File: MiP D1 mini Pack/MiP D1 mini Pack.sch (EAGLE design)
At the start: 6 parts, among them J2 D1 mini, J3 Debug

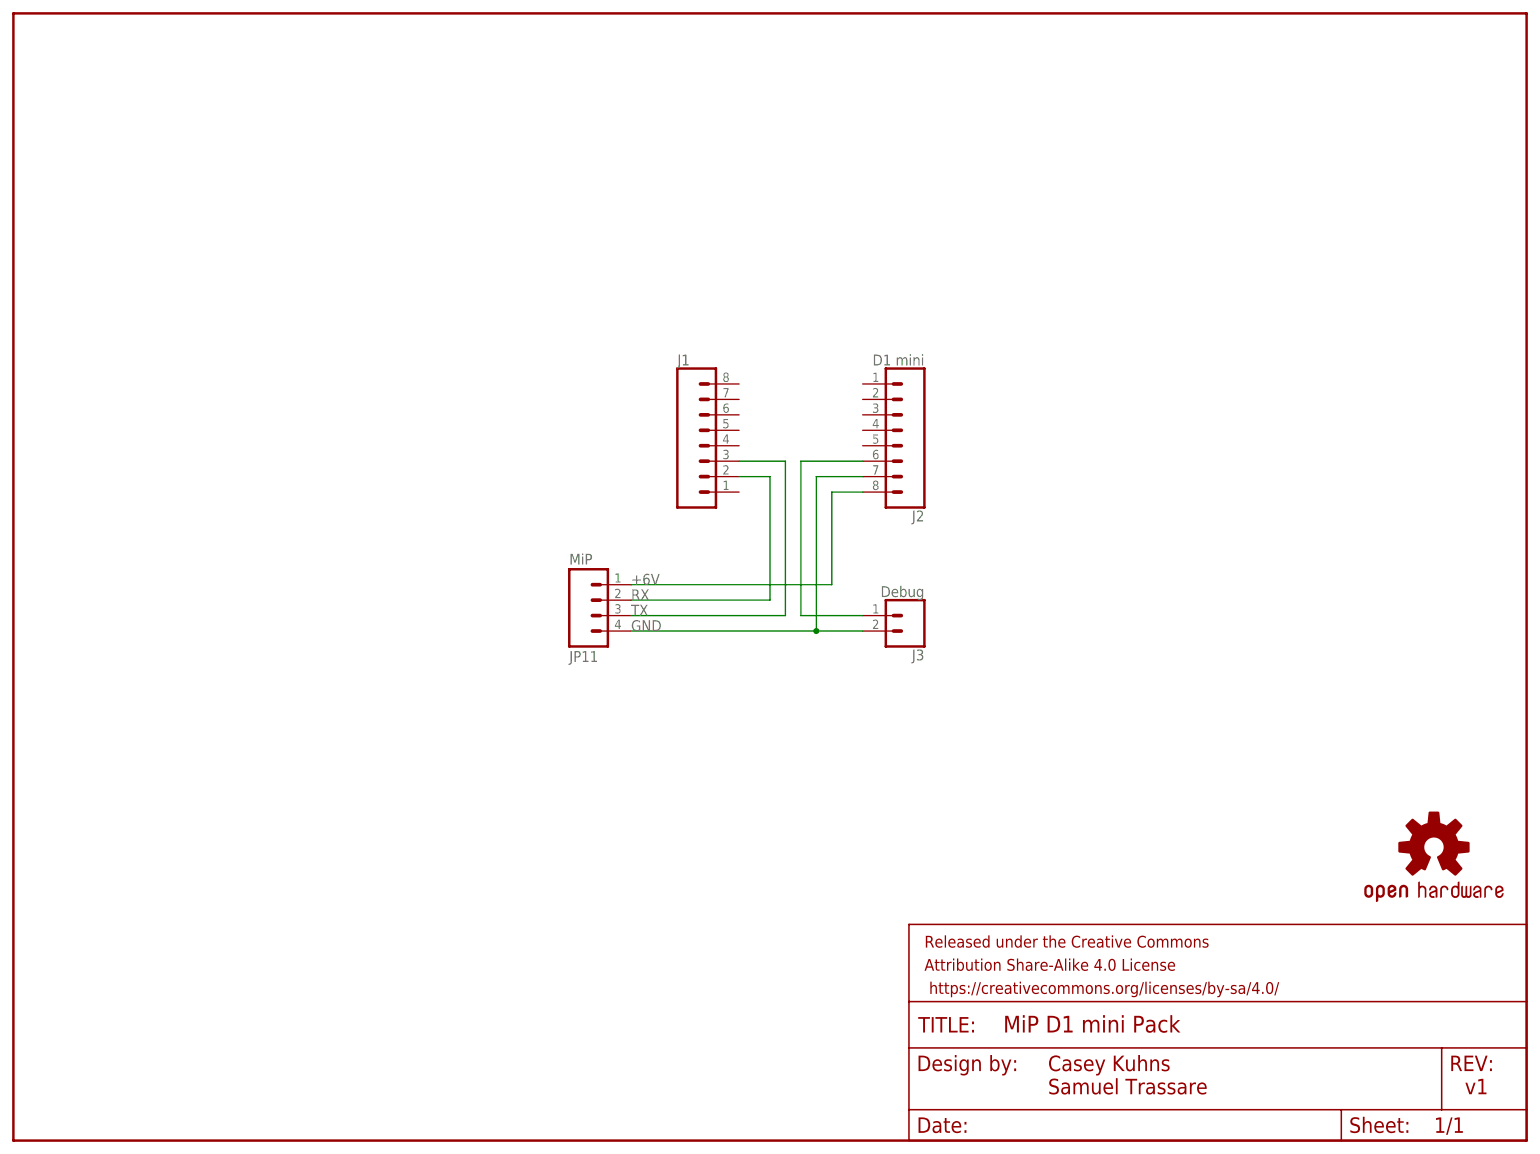
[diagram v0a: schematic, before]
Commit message: Fixed rookie mistake (RX/TX was backwards)
Fixed twisted RX/TX pair, corrected labels, added labels for debug
connector, made minor moves.
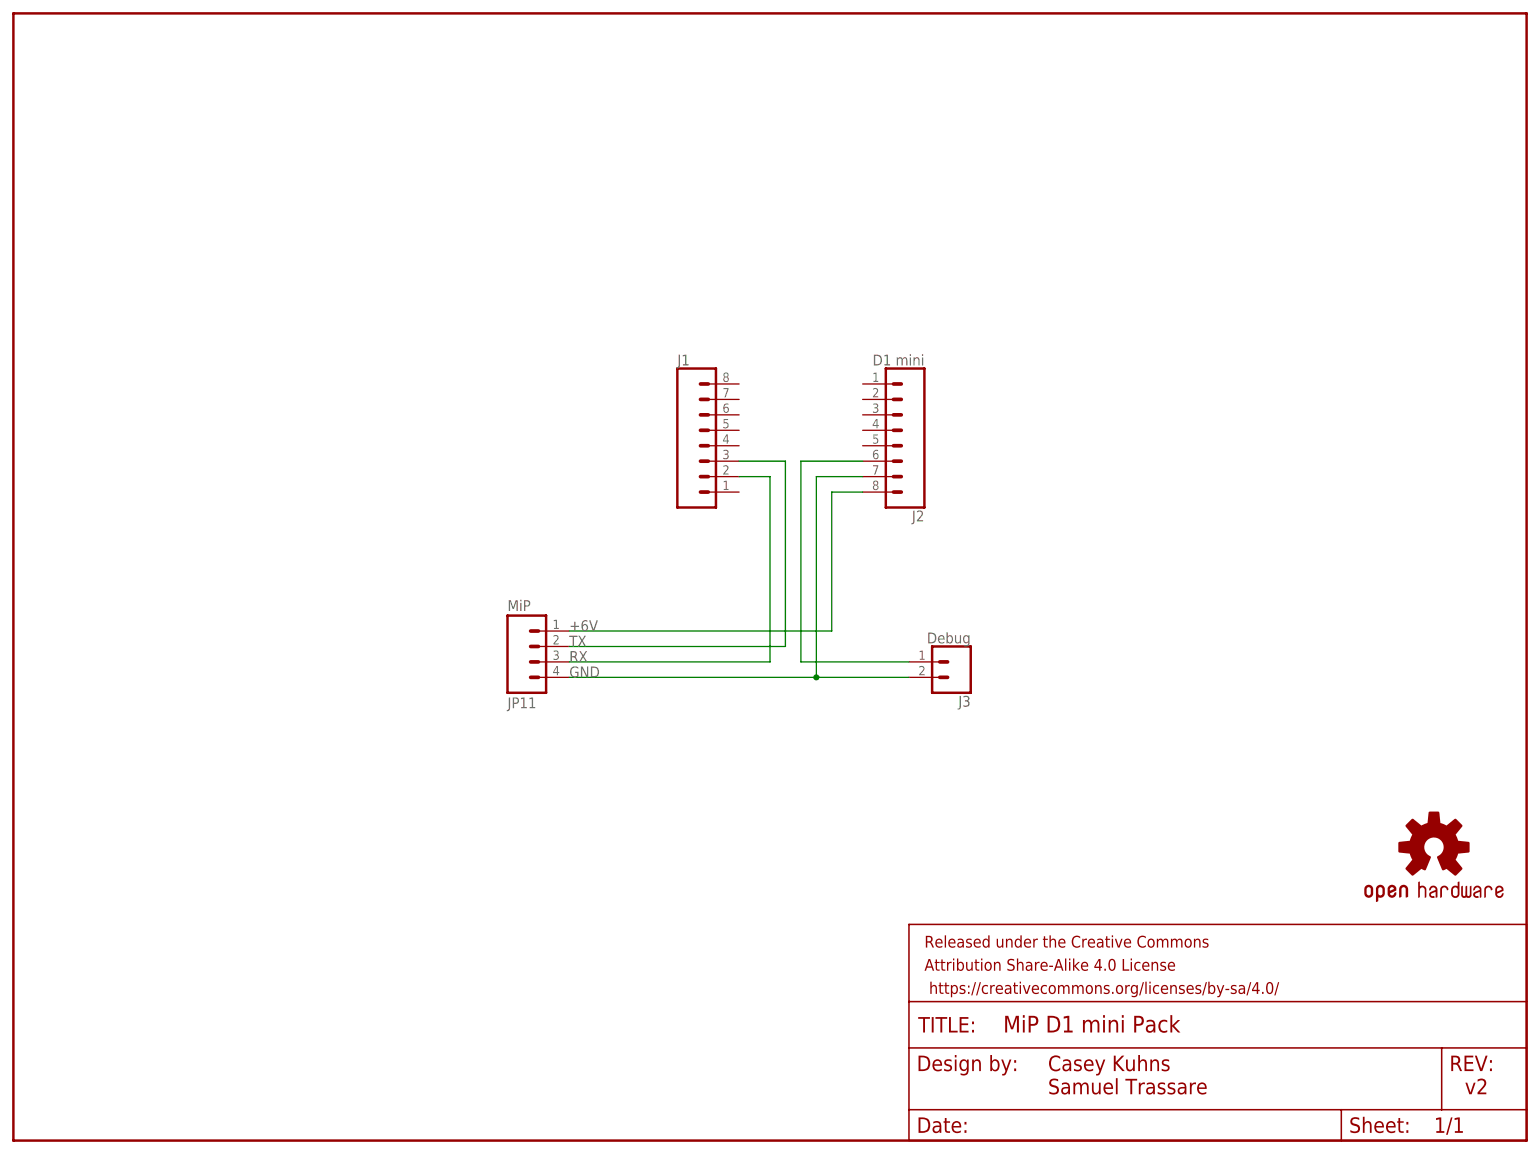
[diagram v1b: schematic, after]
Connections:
- net N$4 renamed DEBUG
- net RX: now also JP11.3; no longer JP11.2
- net TX: now also JP11.2; no longer JP11.3
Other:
- note added: "v2"
- note removed: "v1"
- moved on the sheet: J3, JP11
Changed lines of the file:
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@@
 <text x="170.18" y="7.62" size="2.54" layer="94">Casey Kuhns
 Samuel Trassare</text>
-<text x="238.76" y="7.62" size="2.54" layer="94">v1</text>
+<text x="238.76" y="7.62" size="2.54" layer="94">v2</text>
 </plain>
 <instances>
 <instance part="FRAME1" gate="G$1" x="0" y="0"/>
 <instance part="FRAME1" gate="G$2" x="147.32" y="0"/>
-<instance part="JP11" gate="G$1" x="96.52" y="88.9" rot="MR180"/>
+<instance part="JP11" gate="G$1" x="86.36" y="81.28" rot="MR180"/>
 <instance part="LOGO2" gate="G$1" x="233.68" y="48.26"/>
 <instance part="J1" gate="G$1" x="114.3" y="114.3"/>
 <instance part="J2" gate="G$1" x="144.78" y="116.84" rot="R180"/>
-<instance part="J3" gate="G$1" x="147.32" y="86.36" rot="R180"/>
+<instance part="J3" gate="G$1" x="154.94" y="78.74" rot="R180"/>
 </instances>
 <busses>
 </busses>
 <nets>
-<net name="N$4" class="0">
+<net name="DEBUG" class="0">
 <segment>
 <pinref part="J3" gate="G$1" pin="1"/>
-<wire x1="139.7" y1="86.36" x2="129.54" y2="86.36" width="0.1524" layer="91"/>
-<wire x1="129.54" y1="86.36" x2="129.54" y2="111.76" width="0.1524" layer="91"/>
+<wire x1="147.32" y1="78.74" x2="129.54" y2="78.74" width="0.1524" layer="91"/>
+<wire x1="129.54" y1="78.74" x2="129.54" y2="111.76" width="0.1524" layer="91"/>
 <pinref part="J2" gate="G$1" pin="6"/>
 <wire x1="129.54" y1="111.76" x2="139.7" y2="111.76" width="0.1524" layer="91"/>
@@
 <pinref part="JP11" gate="G$1" pin="4"/>
 <pinref part="J3" gate="G$1" pin="2"/>
-<wire x1="101.6" y1="83.82" x2="132.08" y2="83.82" width="0.1524" layer="91"/>
+<wire x1="91.44" y1="76.2" x2="132.08" y2="76.2" width="0.1524" layer="91"/>
 <pinref part="J2" gate="G$1" pin="7"/>
-<wire x1="132.08" y1="83.82" x2="139.7" y2="83.82" width="0.1524" layer="91"/>
+<wire x1="132.08" y1="76.2" x2="147.32" y2="76.2" width="0.1524" layer="91"/>
 <wire x1="139.7" y1="109.22" x2="132.08" y2="109.22" width="0.1524" layer="91"/>
-<wire x1="132.08" y1="109.22" x2="132.08" y2="83.82" width="0.1524" layer="91"/>
-<junction x="132.08" y="83.82"/>
-<label x="101.6" y="83.82" size="1.778" layer="95"/>
+<wire x1="132.08" y1="109.22" x2="132.08" y2="76.2" width="0.1524" layer="91"/>
+<junction x="132.08" y="76.2"/>
+<label x="91.44" y="76.2" size="1.778" layer="95"/>
 </segment>
 </net>
-<net name="+6V" class="1">
+<net name="RX" class="0">
 <segment>
-<pinref part="JP11" gate="G$1" pin="1"/>
-<wire x1="101.6" y1="91.44" x2="134.62" y2="91.44" width="0.1524" layer="91"/>
-<wire x1="134.62" y1="91.44" x2="134.62" y2="106.68" width="0.1524" layer="91"/>
-<pinref part="J2" gate="G$1" pin="8"/>
-<wire x1="134.62" y1="106.68" x2="139.7" y2="106.68" width="0.1524" layer="91"/>
-<label x="101.6" y="91.44" size="1.778" layer="95"/>
+<pinref part="JP11" gate="G$1" pin="3"/>
+<wire x1="91.44" y1="78.74" x2="124.46" y2="78.74" width="0.1524" layer="91"/>
+<wire x1="124.46" y1="78.74" x2="124.46" y2="109.22" width="0.1524" layer="91"/>
+<pinref part="J1" gate="G$1" pin="2"/>
+<wire x1="124.46" y1="109.22" x2="119.38" y2="109.22" width="0.1524" layer="91"/>
+<label x="91.44" y="78.74" size="1.778" layer="95"/>
 </segment>
 </net>
 <net name="TX" class="0">
 <segment>
-<pinref part="JP11" gate="G$1" pin="3"/>
-<wire x1="101.6" y1="86.36" x2="127" y2="86.36" width="0.1524" layer="91"/>
-<wire x1="127" y1="86.36" x2="127" y2="111.76" width="0.1524" layer="91"/>
+<pinref part="JP11" gate="G$1" pin="2"/>
+<wire x1="91.44" y1="81.28" x2="127" y2="81.28" width="0.1524" layer="91"/>
+<wire x1="127" y1="81.28" x2="127" y2="111.76" width="0.1524" layer="91"/>
 <pinref part="J1" gate="G$1" pin="3"/>
 <wire x1="127" y1="111.76" x2="119.38" y2="111.76" width="0.1524" layer="91"/>
-<label x="101.6" y="86.36" size="1.778" layer="95"/>
+<label x="91.44" y="81.28" size="1.778" layer="95"/>
 </segment>
 </net>
-<net name="RX" class="0">
+<net name="+6V" class="0">
 <segment>
-<pinref part="JP11" gate="G$1" pin="2"/>
-<wire x1="101.6" y1="88.9" x2="124.46" y2="88.9" width="0.1524" layer="91"/>
-<wire x1="124.46" y1="88.9" x2="124.46" y2="109.22" width="0.1524" layer="91"/>
-<pinref part="J1" gate="G$1" pin="2"/>
-<wire x1="124.46" y1="109.22" x2="119.38" y2="109.22" width="0.1524" layer="91"/>
-<label x="101.6" y="88.9" size="1.778" layer="95"/>
+<pinref part="JP11" gate="G$1" pin="1"/>
+<wire x1="91.44" y1="83.82" x2="134.62" y2="83.82" width="0.1524" layer="91"/>
+<wire x1="134.62" y1="83.82" x2="134.62" y2="106.68" width="0.1524" layer="91"/>
+<pinref part="J2" gate="G$1" pin="8"/>
+<wire x1="134.62" y1="106.68" x2="139.7" y2="106.68" width="0.1524" layer="91"/>
+<label x="91.44" y="83.82" size="1.778" layer="95"/>
 </segment>
 </net>
